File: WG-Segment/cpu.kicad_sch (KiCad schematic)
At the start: 1 part, among them U201 RP2040

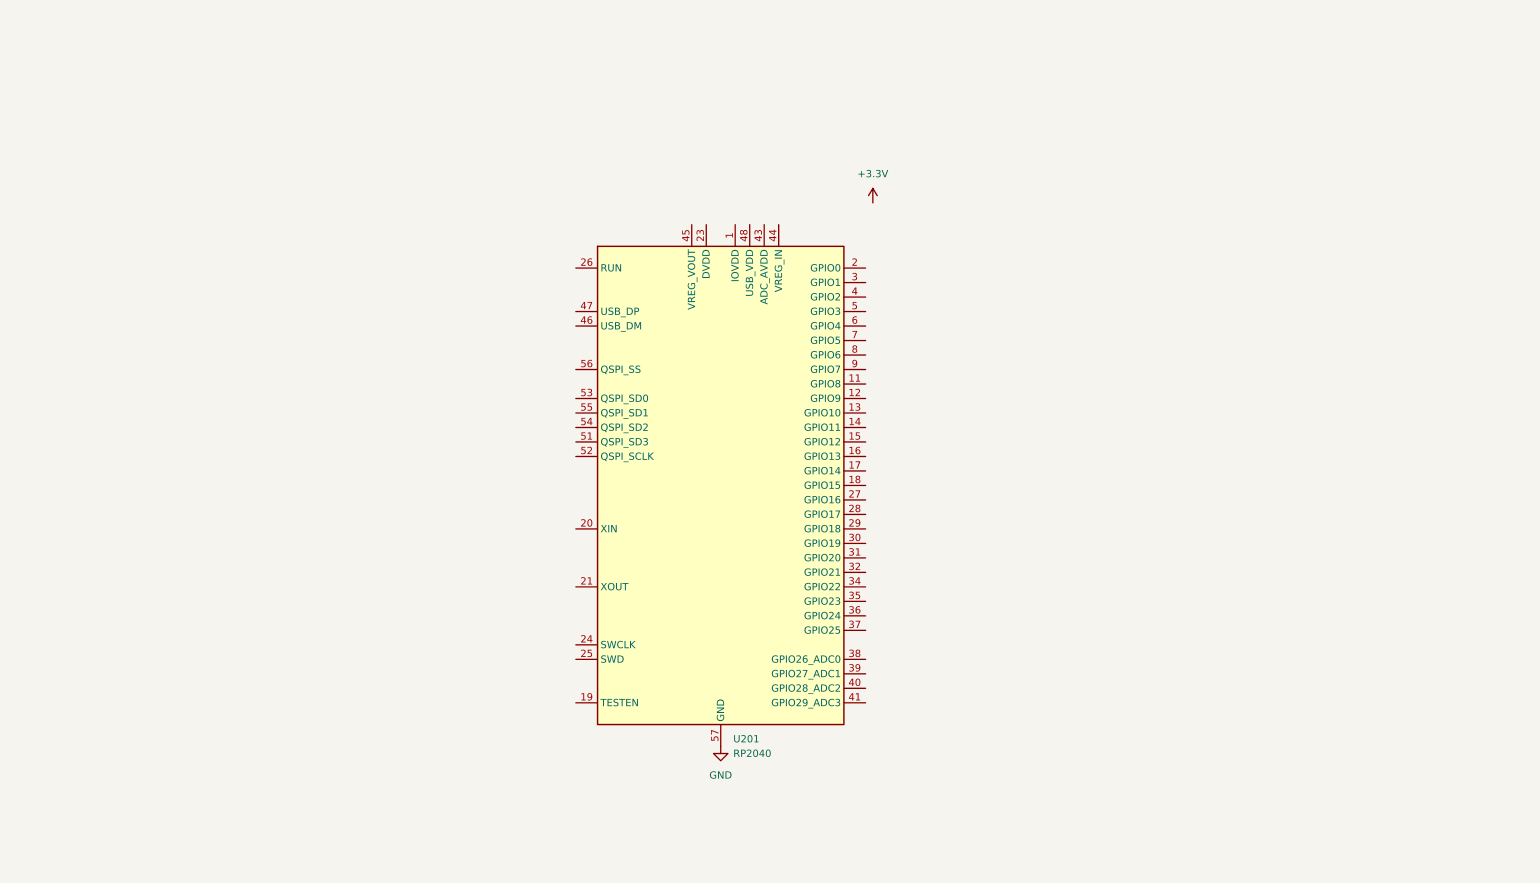
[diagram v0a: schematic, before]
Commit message: Design full circuit
Still need to run ERC
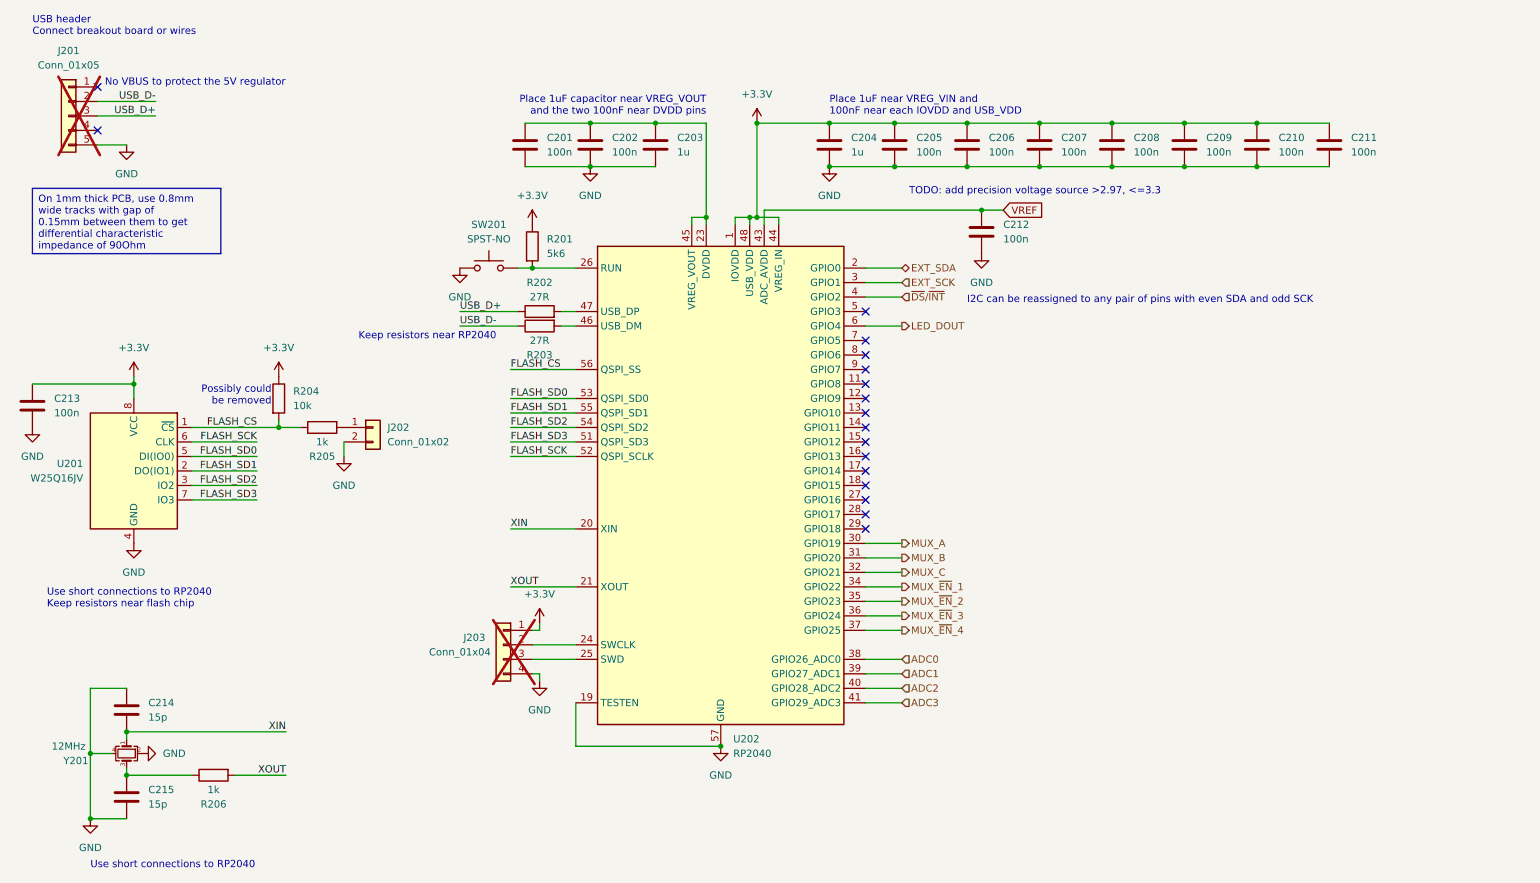
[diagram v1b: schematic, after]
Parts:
- added C201, C202, C205, C206, C207, C208, C209, C210, C211, C212, C213: 100n, Capacitor_SMD:C_0402_1005Metric_Pad0.74x0.62mm_HandSolder, symbol Device:C
- added C203, C204: 1u, Capacitor_SMD:C_0402_1005Metric_Pad0.74x0.62mm_HandSolder, symbol Device:C
- added C214, C215: 15p, Capacitor_SMD:C_0402_1005Metric_Pad0.74x0.62mm_HandSolder, symbol Device:C
- added J201: Conn_01x05, Connector_PinSocket_2.54mm:PinSocket_1x05_P2.54mm_Vertical, symbol Connector_Generic:Conn_01x05
- added J202: Conn_01x02, Connector_PinSocket_2.54mm:PinSocket_1x02_P2.54mm_Vertical, symbol Connector_Generic:Conn_01x02
- added J203: Conn_01x04, Connector_PinHeader_2.54mm:PinHeader_1x04_P2.54mm_Vertical, symbol Connector_Generic:Conn_01x04
- added R201: 5k6, Resistor_SMD:R_0402_1005Metric_Pad0.72x0.64mm_HandSolder, symbol Device:R
- added R202, R203: 27R, Resistor_SMD:R_0402_1005Metric_Pad0.72x0.64mm_HandSolder, symbol Device:R
- added R204: 10k, Resistor_SMD:R_0402_1005Metric_Pad0.72x0.64mm_HandSolder, symbol Device:R
- added R205, R206: 1k, Resistor_SMD:R_0402_1005Metric_Pad0.72x0.64mm_HandSolder, symbol Device:R
- added SW201: SPST-NO, Button_Switch_SMD:SW_SPST_PTS810, symbol Switch:SW_Push
- added U201: W25Q16JV, Package_SO:SOIC-8_5.23x5.23mm_P1.27mm, symbol Memory_Flash:W25Q128JVS
- added Y201: 12MHz, Crystal:Crystal_SMD_Abracon_ABM8G-4Pin_3.2x2.5mm, symbol Device:Crystal_GND24_Small
- U202: renamed from U201; Manufacturer (none) -> Raspberry Pi; Part Number (none) -> RP2040
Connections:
- net +3.3V: now also U202.1 (IOVDD), U202.10 (IOVDD), U202.22 (IOVDD), U202.33 (IOVDD), U202.42 (IOVDD), U202.44 (VREG_IN), U202.48 (USB_VDD), U202.49 (IOVDD), C204.1, C205.1, C206.1, C207.1, C208.1, C209.1, C210.1, C211.1, C213.1, J203.1 (Pin_1), R201.1, R204.1, U201.8 (VCC)
- net GND: now also U202.19 (TESTEN), C201.2, C202.2, C203.2, C204.2, C205.2, C206.2, C207.2, C208.2, C209.2, C210.2, C211.2, C212.2, C213.2, C214.1, C215.2, J201.5 (Pin_5), J202.2 (Pin_2), J203.4 (Pin_4), SW201.1, U201.4 (GND), Y201.2, Y201.4
- net EXT_SDA: now reaches U202.2 (GPIO0)
- net XIN: now reaches U202.20 (XIN)
- net XIN: now also C214.2, Y201.1
- net XOUT: now reaches U202.21 (XOUT)
- net XOUT: now also R206.2
- net at U202.23 (DVDD), U202.50 (DVDD): now also U202.45 (VREG_VOUT), C201.1, C202.1, C203.1
- net at U202.24 (SWCLK): now also J203.2 (Pin_2)
- net at U202.25 (SWD): now also J203.3 (Pin_3)
- net at U202.26 (RUN): now also R201.2, SW201.2
- net EXT_SCK: now reaches U202.3 (GPIO1)
- net MUX_A: now reaches U202.30 (GPIO19)
- net MUX_B: now reaches U202.31 (GPIO20)
- net MUX_C: now reaches U202.32 (GPIO21)
- net MUX_~{EN}_1: now reaches U202.34 (GPIO22)
- net MUX_~{EN}_2: now reaches U202.35 (GPIO23)
- net MUX_~{EN}_3: now reaches U202.36 (GPIO24)
- net MUX_~{EN}_4: now reaches U202.37 (GPIO25)
- net ADC0: now reaches U202.38 (GPIO26_ADC0)
- net ADC1: now reaches U202.39 (GPIO27_ADC1)
- net ~{DS}/~{INT}: now reaches U202.4 (GPIO2)
- net ADC2: now reaches U202.40 (GPIO28_ADC2)
- net ADC3: now reaches U202.41 (GPIO29_ADC3)
- net VREF: now reaches U202.43 (ADC_AVDD)
- net VREF: now also C212.1
- net at U202.46 (USB_DM): now also R203.2
- net at U202.47 (USB_DP): now also R202.2
- net FLASH_SD3: now reaches U202.51 (QSPI_SD3)
- net FLASH_SD3: now also U201.7 (IO3)
- net FLASH_SCK: now reaches U202.52 (QSPI_SCLK)
- net FLASH_SCK: now also U201.6 (CLK)
- net FLASH_SD0: now reaches U202.53 (QSPI_SD0)
- net FLASH_SD0: now also U201.5 (DI(IO0))
- net FLASH_SD2: now reaches U202.54 (QSPI_SD2)
- net FLASH_SD2: now also U201.3 (IO2)
- net FLASH_SD1: now reaches U202.55 (QSPI_SD1)
- net FLASH_SD1: now also U201.2 (DO(IO1))
- net FLASH_CS: now reaches U202.56 (QSPI_SS)
- net FLASH_CS: now also R204.2, R205.1, U201.1 (~{CS})
- net LED_DOUT: now reaches U202.6 (GPIO4)
- new net: J202.1 (Pin_1), R205.2
- new net: C215.1, R206.1, Y201.3
- new net USB_D+: J201.3 (Pin_3), R202.1
- new net USB_D-: J201.2 (Pin_2), R203.1
- no-connect marks 0 -> 17
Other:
- note added: "I2C can be reassigned to any pair of pins with even SDA and odd SCK"
- note added: "Keep resistors near RP2040"
- note added: "No VBUS to protect the 5V regulator"
- note added: "Place 1uF capacitor near VREG_VOUT and the two 100nF near DVDD pins"
- note added: "Place 1uF near VREG_VIN and 100nF near each IOVDD and USB_VDD"
- note added: "Possibly could be removed"
- note added: "TODO: add precision voltage source >2.97, <=3.3"
- note added: "USB header Connect breakout board or wires"
- note added: "Use short connections to RP2040"
- note added: "Use short connections to RP2040 Keep resistors near flash chip"

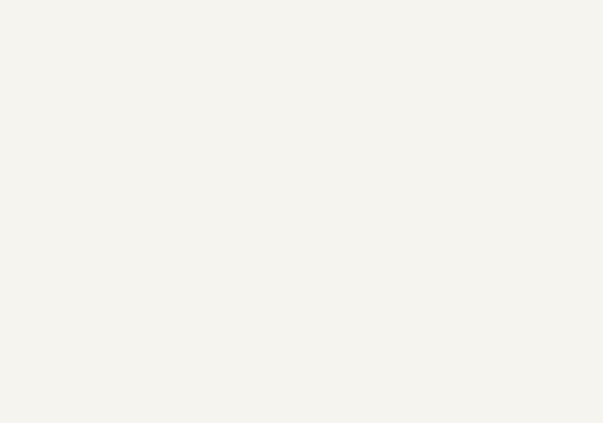
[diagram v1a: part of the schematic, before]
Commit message: Add level shifter to LED data input
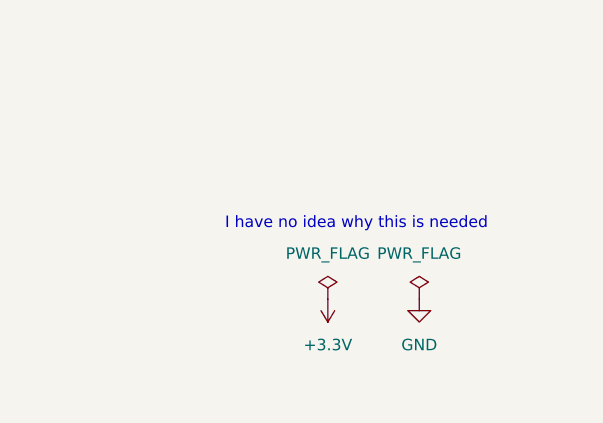
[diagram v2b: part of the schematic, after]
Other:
- note added: "I have no idea why this is needed"

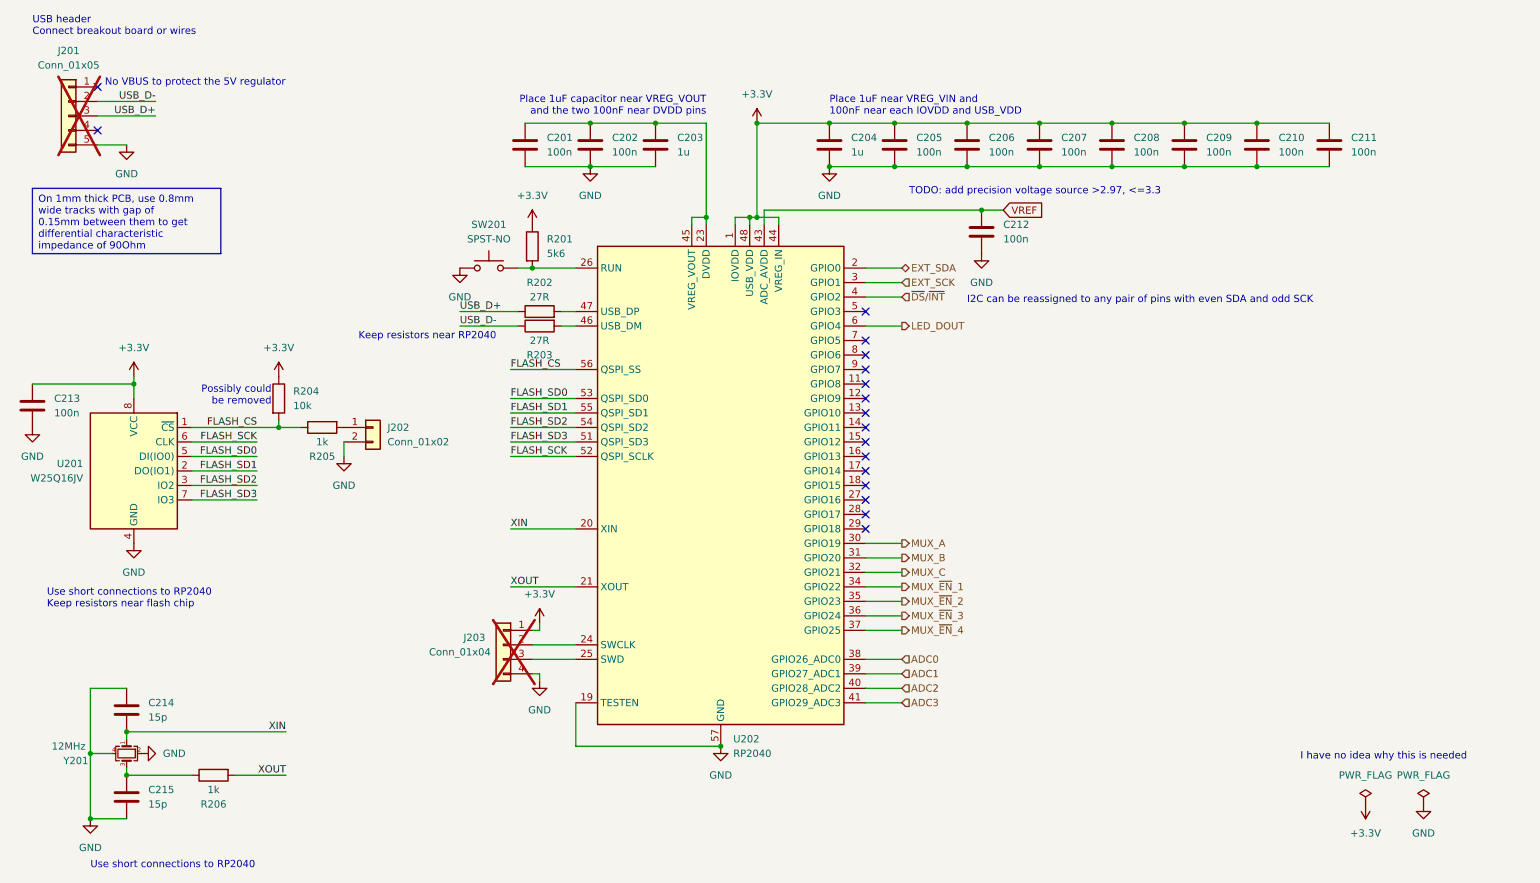
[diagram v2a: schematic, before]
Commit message: Position power circuitry
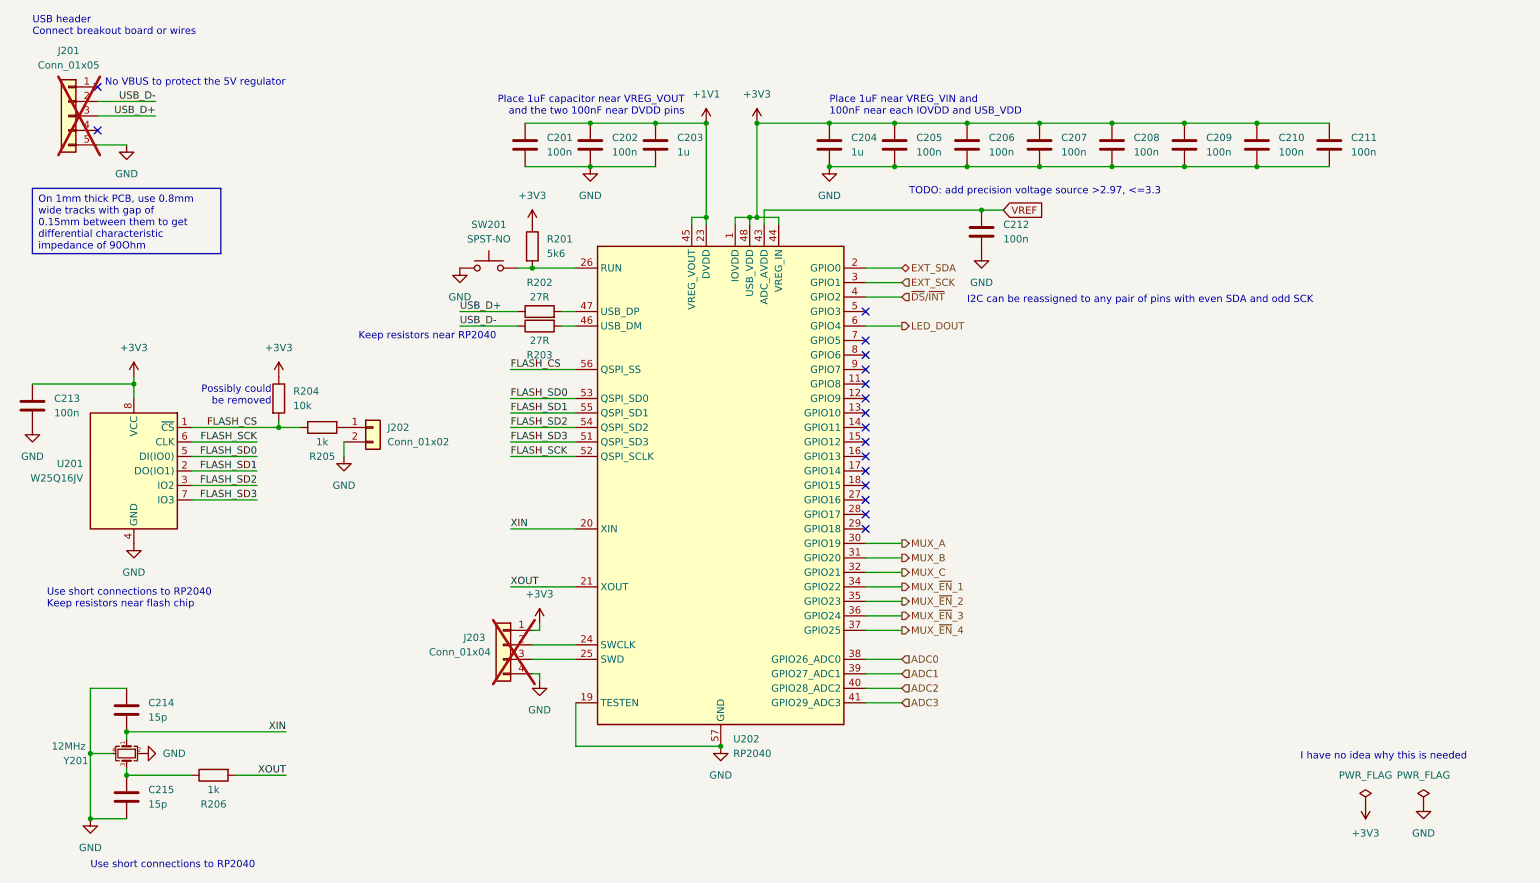
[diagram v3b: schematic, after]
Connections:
- net +1V1: now reaches C201.1, C202.1, C203.1, U202.23 (DVDD), U202.45 (VREG_VOUT), U202.50 (DVDD)
- net +3.3V renamed +3V3

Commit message: Finish designing most of the PCB
Only need to connect analog traces. May need to make the board a 4-layer PCB
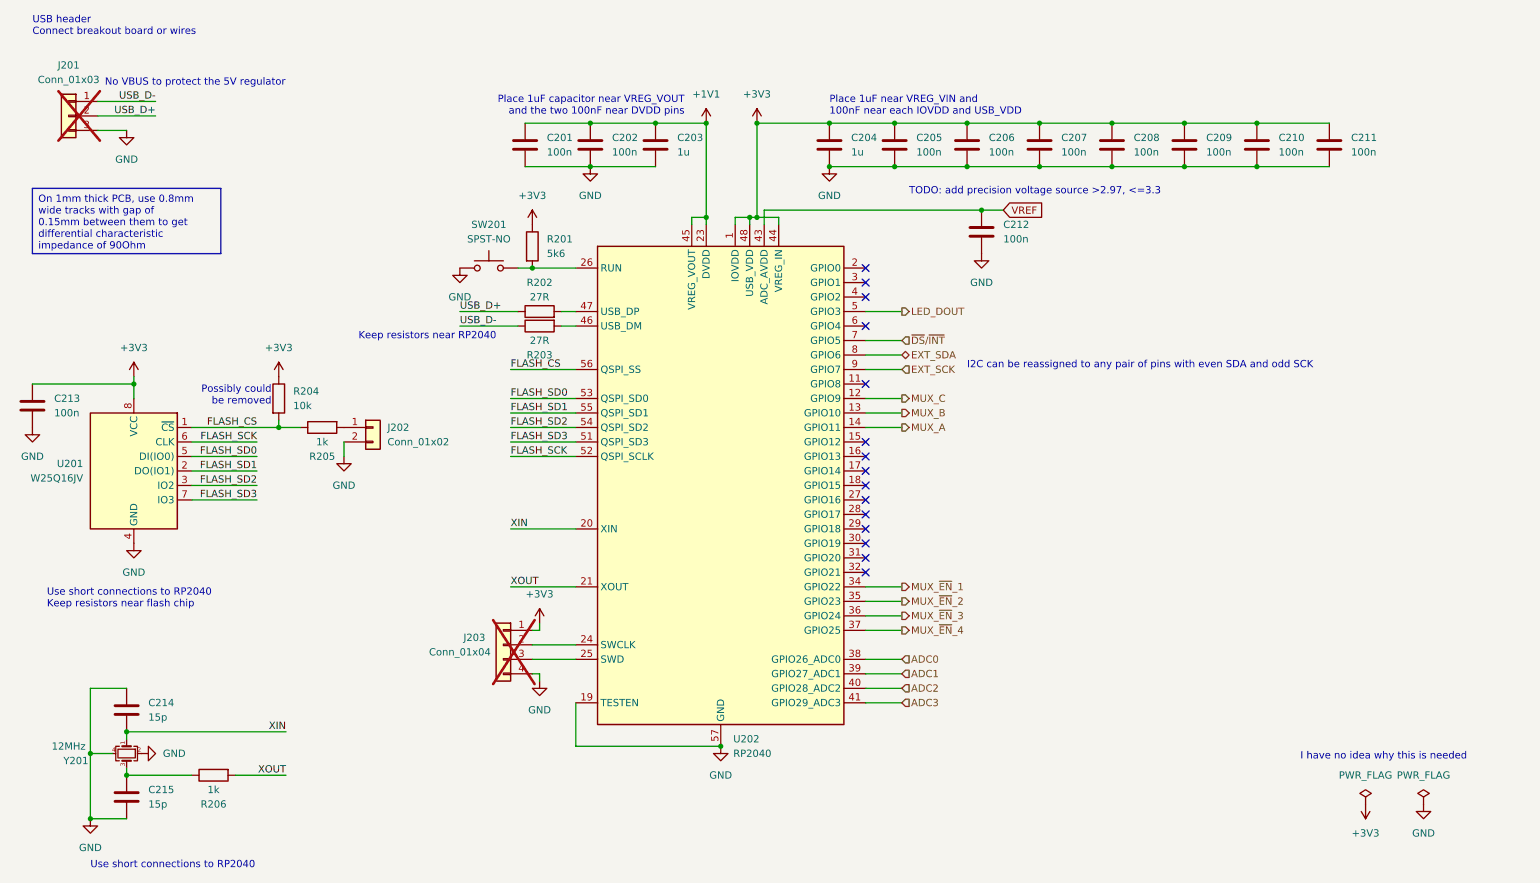
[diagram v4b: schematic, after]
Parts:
- removed J201: Conn_01x05, Connector_PinSocket_2.54mm:PinSocket_1x05_P2.54mm_Vertical, symbol Connector_Generic:Conn_01x05
- added J201: Conn_01x03, Connector_PinHeader_2.54mm:PinHeader_1x03_P2.54mm_Vertical, symbol Connector_Generic:Conn_01x03
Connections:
- net EXT_SCK: now also U202.9 (GPIO7); no longer U202.3 (GPIO1)
- net EXT_SDA: now also U202.8 (GPIO6); no longer U202.2 (GPIO0)
- net GND: now also J201.3 (Pin_3)
- net LED_DOUT: now also U202.5 (GPIO3); no longer U202.6 (GPIO4)
- net MUX_A: now also U202.14 (GPIO11); no longer U202.30 (GPIO19)
- net MUX_B: now also U202.13 (GPIO10); no longer U202.31 (GPIO20)
- net MUX_C: now also U202.12 (GPIO9); no longer U202.32 (GPIO21)
- net USB_D+: now also J201.2 (Pin_2)
- net USB_D-: now also J201.1 (Pin_1)
- net ~{DS}/~{INT}: now also U202.7 (GPIO5); no longer U202.4 (GPIO2)
- no-connect marks 17 -> 15

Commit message: Add ADC-tile connections
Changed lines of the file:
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@@
-    )
-  )
-  (symbol (lib_id "power:PWR_FLAG") (at 259.08 154.94 0) (unit 1)
-    (in_bom yes) (on_board yes) (dnp no) (fields_autoplaced)
-    (property "Reference" "#FLG0201" (at 259.08 153.035 0)
-      (effects (font (size 1.27 1.27)) hide)
-    )
-    (property "Value" "PWR_FLAG" (at 259.08 149.86 0)
-      (effects (font (size 1.27 1.27)))
-    )
-    (property "Footprint" "" (at 259.08 154.94 0)
-      (effects (font (size 1.27 1.27)) hide)
-    )
-    (property "Datasheet" "~" (at 259.08 154.94 0)
-      (effects (font (size 1.27 1.27)) hide)
-    )
-    (pin "1")
-    (instances
-      (project "WG-Segment"
-        (path "/9a5339e6-f970-4986-a2cb-f70ab323b7e1/1e0e1cdf-3136-4548-bd2e-0b31b8fba863"
-          (reference "#FLG0201") (unit 1)
-        )
-      )
     )
   )
@@
         )
       )
-    )
-  )
-  (symbol (lib_id "power:+3V3") (at 259.08 154.94 180) (unit 1)
-    (in_bom yes) (on_board yes) (dnp no) (fields_autoplaced)
-    (property "Reference" "#PWR0110" (at 259.08 151.13 0)
-      (effects (font (size 1.27 1.27)) hide)
-    )
-    (property "Value" "+3V3" (at 259.08 160.02 0)
-      (effects (font (size 1.27 1.27)))
-    )
-    (property "Footprint" "" (at 259.08 154.94 0)
-      (effects (font (size 1.27 1.27)) hide)
-    )
-    (property "Datasheet" "" (at 259.08 154.94 0)
-      (effects (font (size 1.27 1.27)) hide)
-    )
-    (pin "1")
-    (instances
-      (project "WG-Segment"
-        (path "/9a5339e6-f970-4986-a2cb-f70ab323b7e1/1e0e1cdf-3136-4548-bd2e-0b31b8fba863"
-          (reference "#PWR0110") (unit 1)
-        )
-      )

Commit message: Remote TODO
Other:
- note removed: "TODO: add precision voltage source >2.97, <=3.3"
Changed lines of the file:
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@@
-    (effects (font (size 1.27 1.27)) (justify left bottom))
-  )
-  (text "TODO: add precision voltage source >2.97, <=3.3" (at 179.07 48.26 0)
     (effects (font (size 1.27 1.27)) (justify left bottom))
   )
